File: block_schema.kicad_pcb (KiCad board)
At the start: 2 copper layers, 109.6 x 81.8 mm, 79 parts, among them J1 USB_C_Receptacle, J2 SMA, J3 AVR-ISP-6, J4 Monitor Power, J5 Monitor Video, Q1 AO3401A, Q2 BC817, U1 MT3608, U2 MT3608, U3 TP4056, U4 ATmega328P-AU, U5 CP2102, U6 LM1881, Y1 Crystal

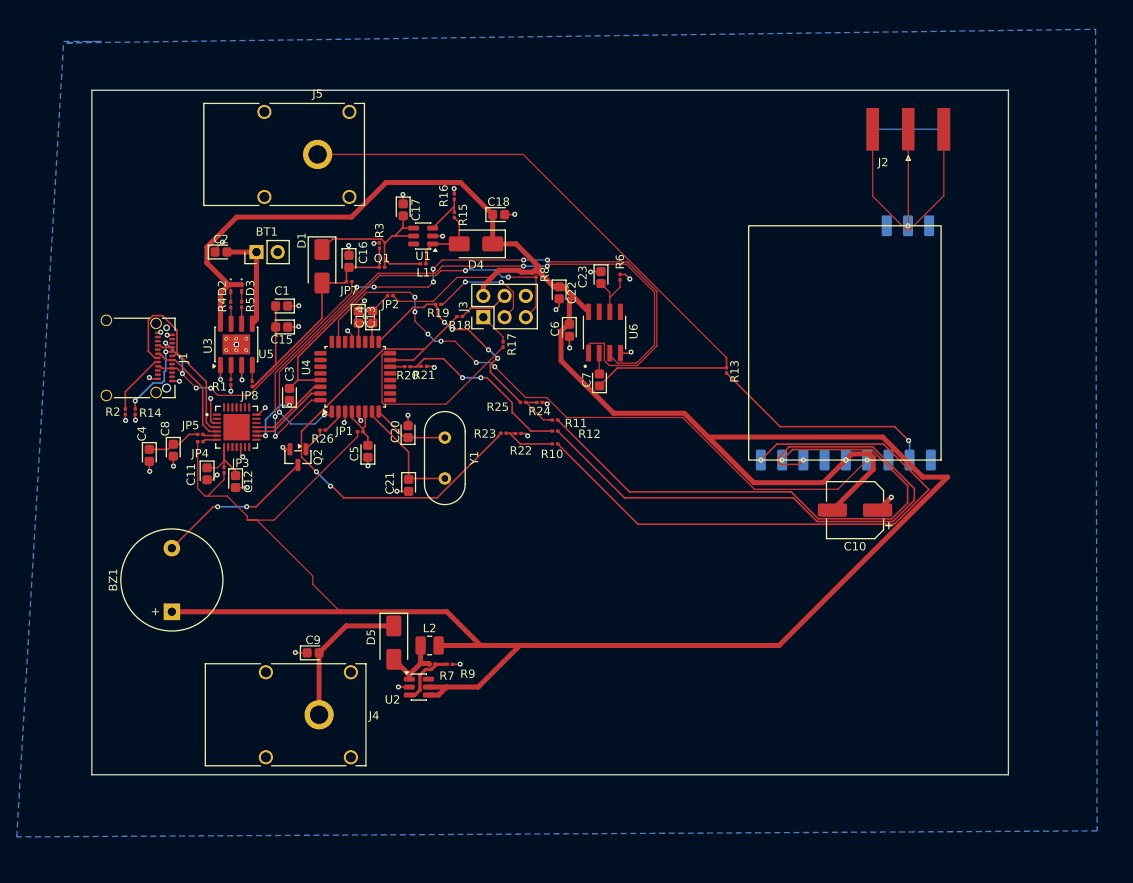
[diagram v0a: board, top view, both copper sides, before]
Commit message: added nestling for pcb and made some improvements in video line
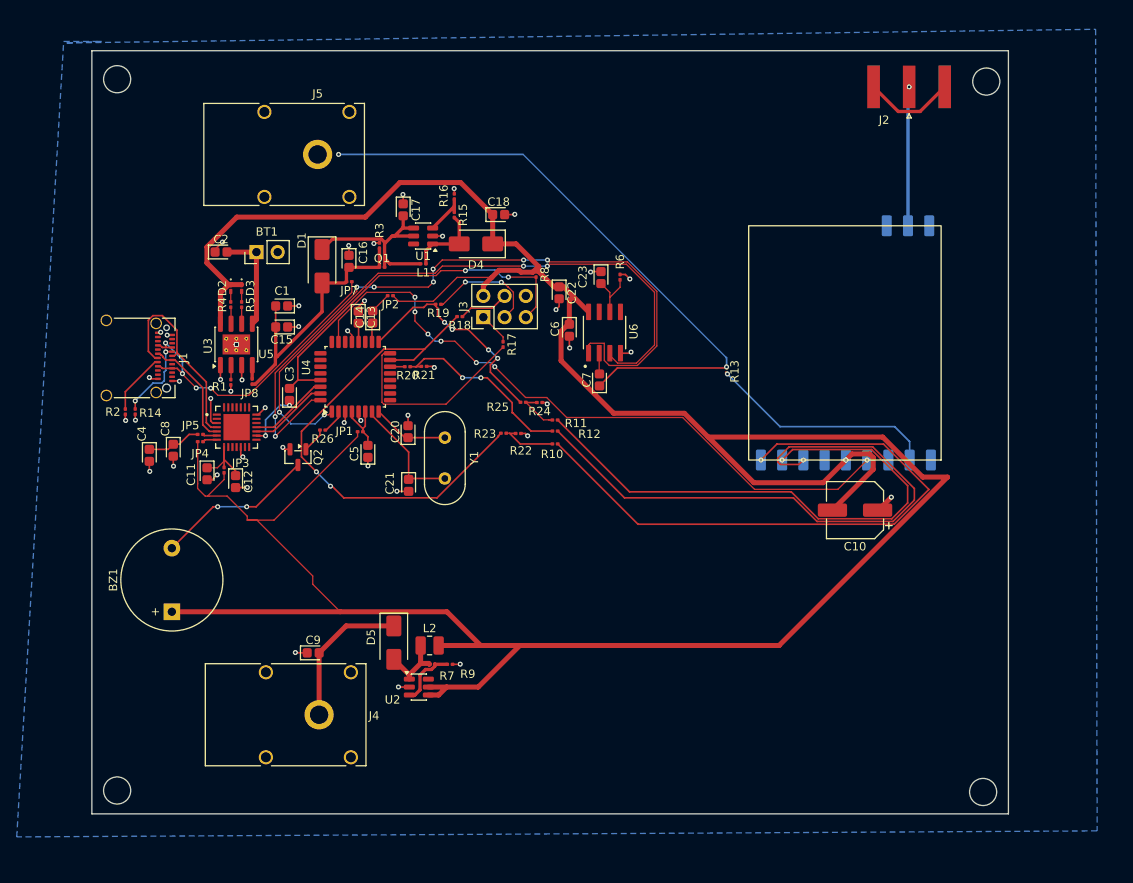
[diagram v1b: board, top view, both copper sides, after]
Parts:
- moved J2 5.06 mm to (173.4, 44.2)
- moved JP8 0.28 mm to (94.9, 79.4)
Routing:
- net Net-(AE1-A): track 36.3 -> 10.9 mm
- net Net-(J2-In): track 11.6 -> 16.7 mm
- net /Power Source/Charge: track 37.4 -> 32.7 mm
- net /MCU (Arduino UNO or NANO)/VIDEO: track 76.2 -> 73.8 mm, vias 0 -> 2
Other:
- board size 109.6 x 81.8 mm -> 109.6 x 91.2 mm

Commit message: added gnd to front layer and made some vias to gnd
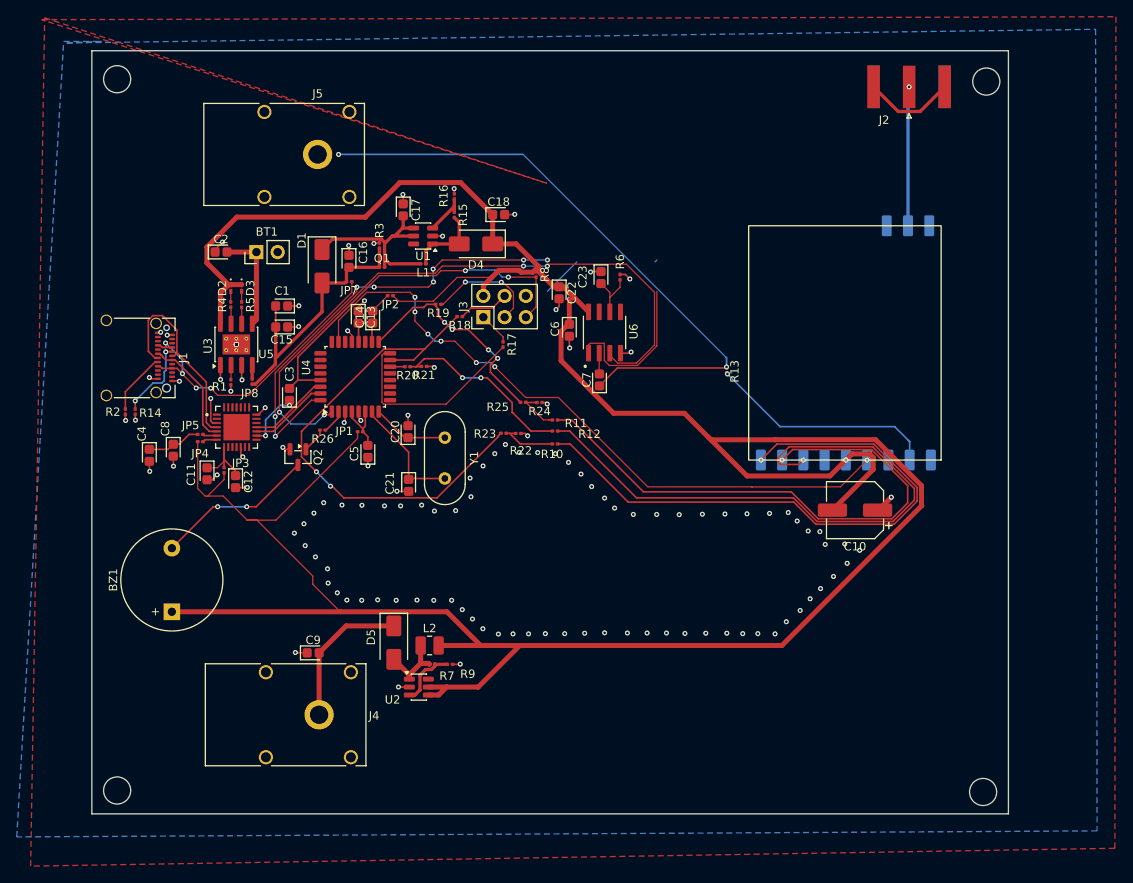
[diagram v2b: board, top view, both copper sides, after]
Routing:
- net /MCU (Arduino UNO or NANO)/H-Sync: track 87.8 -> 78.5 mm
- net +5V: track 358.7 -> 353.1 mm
- net Net-(U7-CH1): track 73.2 -> 71.3 mm
- net GND: vias 52 -> 127
- added copper zone on F.Cu, net GND

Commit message: fixed some things
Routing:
- net GND: vias 127 -> 102
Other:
- outline, holes or cut-outs redrawn

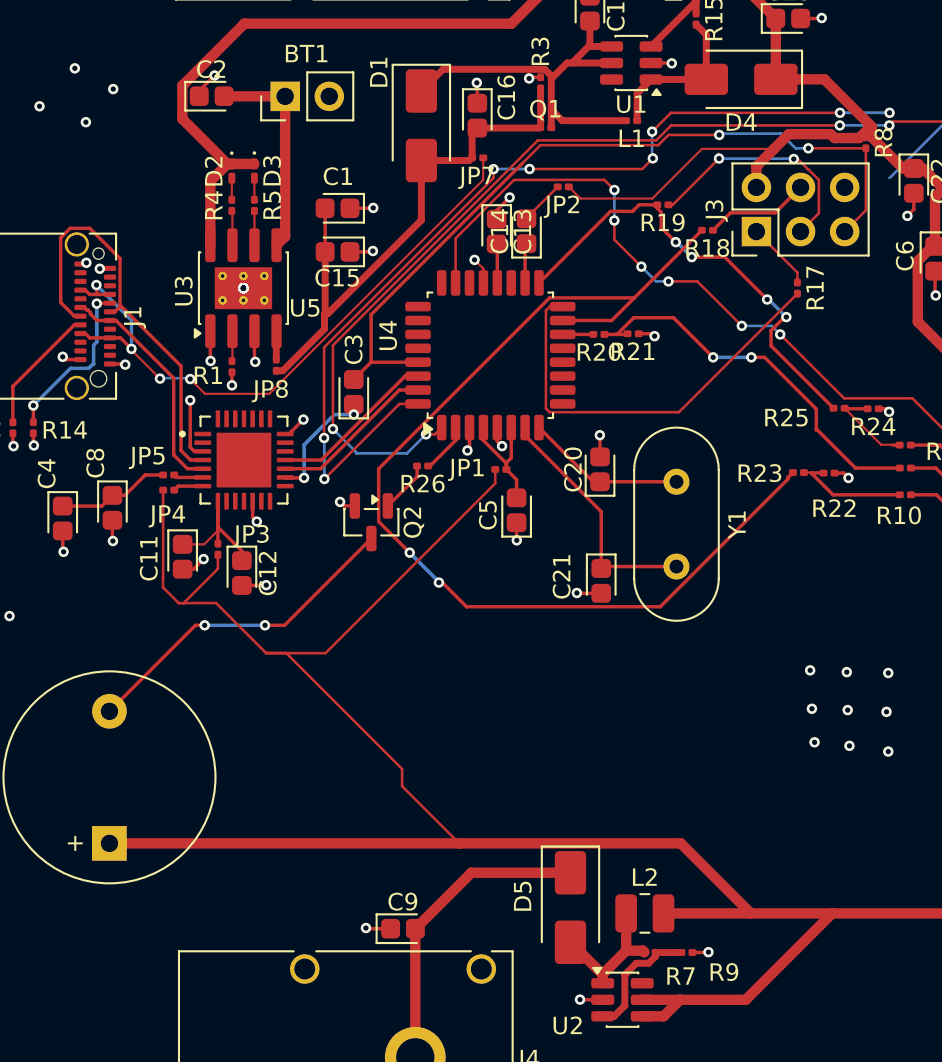
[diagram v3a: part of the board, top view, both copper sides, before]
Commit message: added some decoupling capacitors on power supply
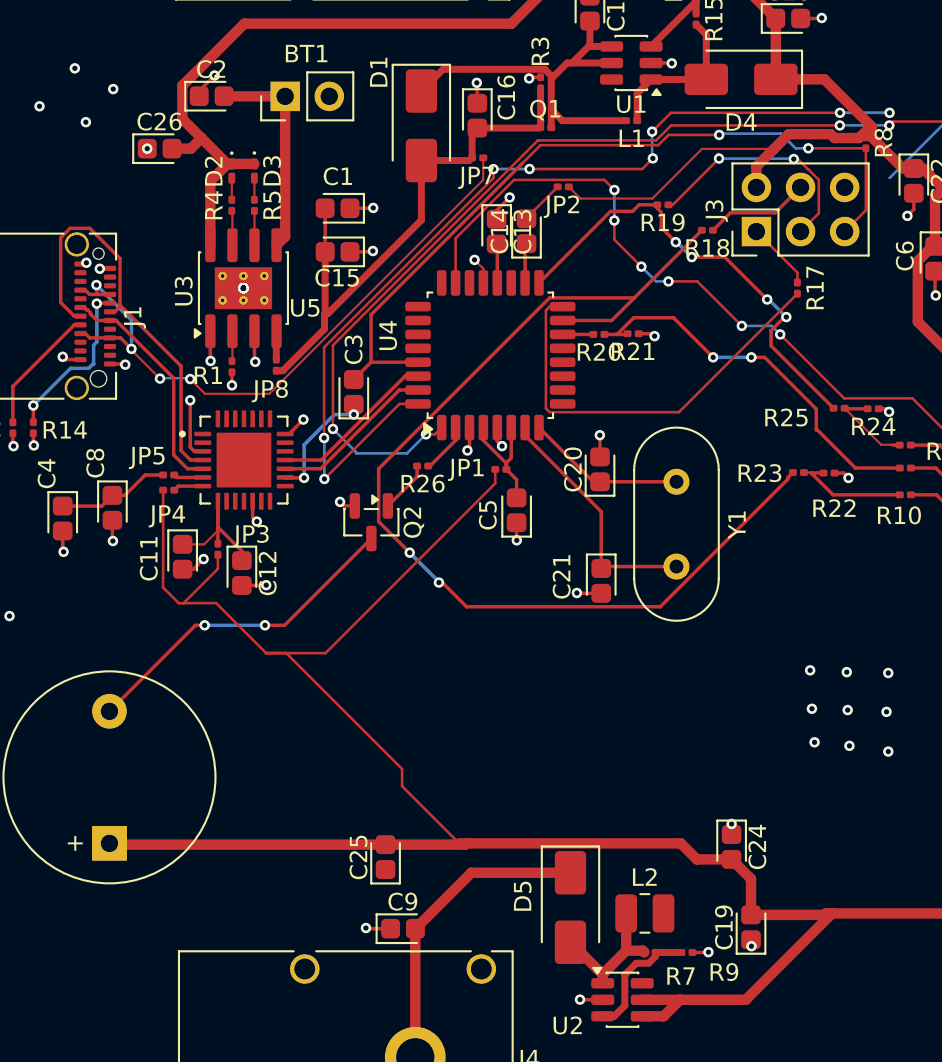
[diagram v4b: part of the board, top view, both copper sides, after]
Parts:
- added C19: 100n, Capacitor_Tantalum_SMD:CP_EIA-1608-08_AVX-J, F.Cu at (122.2, 111.8)
- added C24: 10u, Capacitor_Tantalum_SMD:CP_EIA-1608-08_AVX-J, F.Cu at (121.1, 107.2)
- added C25: 100n, Capacitor_Tantalum_SMD:CP_EIA-1608-08_AVX-J, F.Cu at (101.2, 107.7)
- added C26: 10u, Capacitor_Tantalum_SMD:CP_EIA-1608-08_AVX-J, F.Cu at (88.2, 67.0)
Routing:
- net +5V: track 353.1 -> 351.8 mm
- net GND: track 63.8 -> 64.8 mm, vias 102 -> 105

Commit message: final
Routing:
- net /MCU (Arduino UNO or NANO)/H-Sync: track 78.5 -> 87.8 mm
- net +5V: track 351.8 -> 351.2 mm
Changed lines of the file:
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@@
 	)
 	(segment
-		(start 102.12 102.68)
-		(end 102.12 103.67)
-		(width 0.15)
-		(layer "F.Cu")
-		(net "+5V")
-	)
-	(segment
 		(start 91.085 72.535)
 		(end 91.085 68.849438)
@@
 	)
 	(segment
+		(start 94.304264 96.006064)
+		(end 105.2582 106.96)
+		(width 0.15)
+		(layer "F.Cu")
+		(net "+5V")
+	)
+	(segment
 		(start 133.2425 69.2675)
 		(end 133.2425 69.3175)
@@
 	)
 	(segment
-		(start 94.29 96.006064)
-		(end 95.446064 96.006064)
+		(start 105.2582 106.96)
+		(end 105.41 106.96)
 		(width 0.15)
 		(layer "F.Cu")
@@
 	)
 	(segment
+		(start 94.29 96.006064)
+		(end 94.304264 96.006064)
+		(width 0.15)
+		(layer "F.Cu")
+		(net "+5V")
+	)
+	(segment
 		(start 131.57 68.12)
 		(end 130.948062 68.12)
@@
 	)
 	(segment
-		(start 102.12 103.67)
-		(end 105.41 106.96)
-		(width 0.15)
-		(layer "F.Cu")
-		(net "+5V")
-	)
-	(segment
 		(start 157.359023 86.405686)
 		(end 157.37471 86.39)
@@
 		(net "+5V")
 	)
-	(segment
-		(start 95.446064 96.006064)
-		(end 102.12 102.68)
-		(width 0.15)
-		(layer "F.Cu")
-		(net "+5V")
-	)
 	(via
 		(at 165.845 88.825)
@@
 	)
 	(segment
+		(start 130.173358 64.917257)
+		(end 139.498995 64.917257)
+		(width 0.15)
+		(layer "F.Cu")
+		(net "/MCU (Arduino UNO or NANO)/H-Sync")
+	)
+	(segment
 		(start 115.93795 68.15205)
 		(end 109.455234 68.15205)
@@
 	)
 	(segment
+		(start 139.498995 64.917257)
+		(end 143.247 68.665262)
+		(width 0.15)
+		(layer "F.Cu")
+		(net "/MCU (Arduino UNO or NANO)/H-Sync")
+	)
+	(segment
 		(start 140.922738 77.519)
 		(end 143.247 75.194737)
@@
 		(width 0.15)
 		(layer "B.Cu")
-		(net "/MCU (Arduino UNO or NANO)/H-Sync")
-	)
-	(segment
-		(start 143.022121 65.142136)
-		(end 143.247 64.917257)
-		(width 0.15)
-		(layer "B.Cu")
-		(net "/MCU (Arduino UNO or NANO)/H-Sync")
-	)
-	(segment
-		(start 130.173358 68.665262)
-		(end 133.696484 65.142136)
-		(width 0.15)
-		(layer "B.Cu")
